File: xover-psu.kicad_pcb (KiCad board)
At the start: 2 copper layers, 100 x 100 mm, 91 parts, among them J1 Screw_Terminal_01x02, J2 Screw_Terminal_01x02, J3 Screw_Terminal_01x02, J4 Screw_Terminal_01x02, J5 Screw_Terminal_01x03, J6 Screw_Terminal_01x02, J7 Screw_Terminal_01x02, J8 Screw_Terminal_01x03, K2 T9GS1L14-12, Q1 AO3400, Q2 2N7002, Q3 AO3400, U1 817C, U2 TL431DBZ, U4 LM317_3PinPackage, U5 LM337_TO220, U6 TL431DBZ, U8 817C

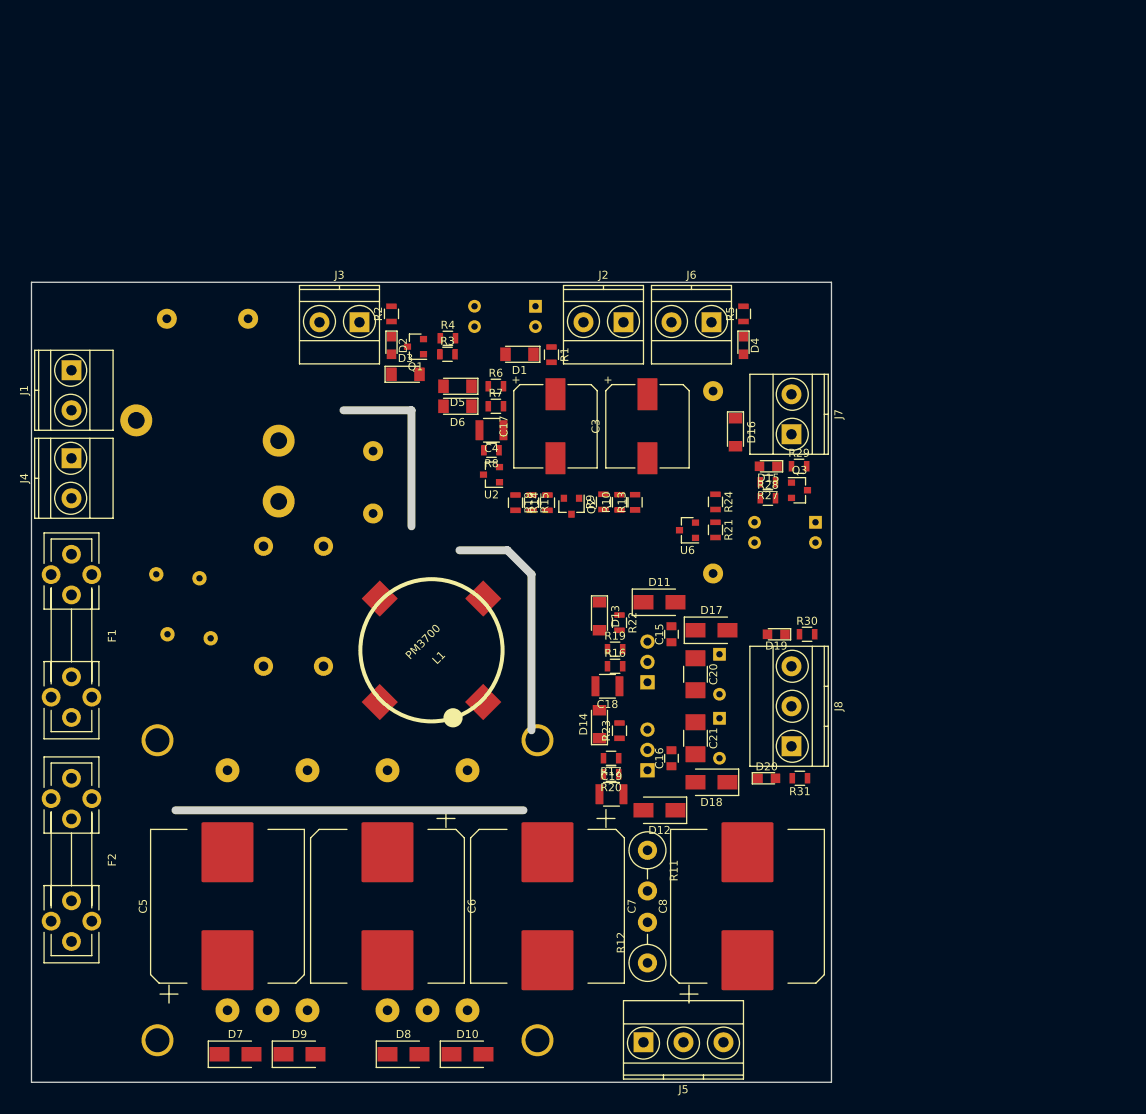
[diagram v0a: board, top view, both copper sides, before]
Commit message: First pass routing completed for all but the UNMUTE timer/logic
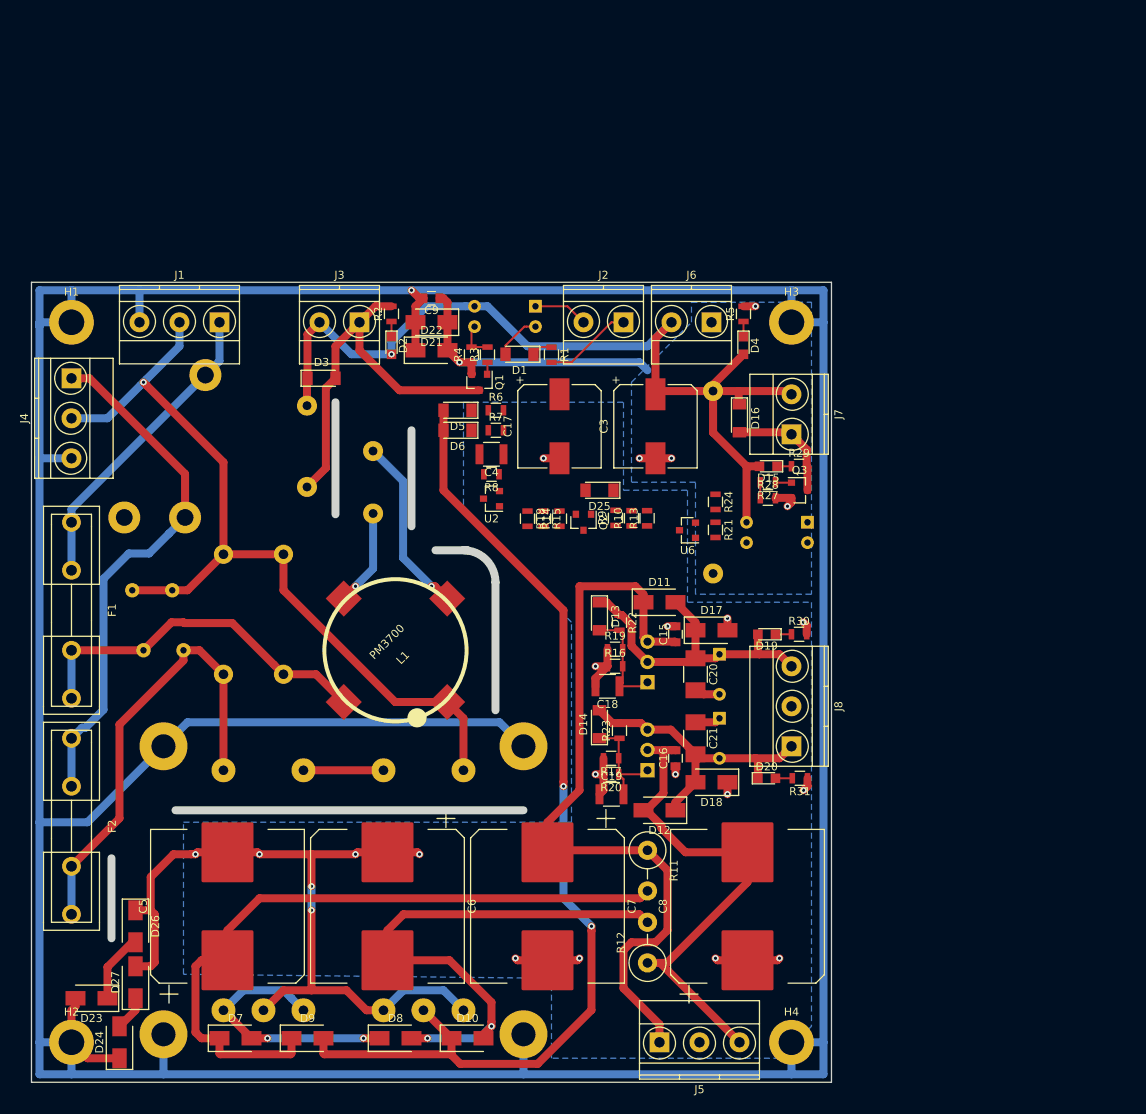
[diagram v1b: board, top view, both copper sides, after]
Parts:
- added C9: 100n, Capacitors_SMD:C_0805, F.Cu at (75.0, 27.0)
- added D21: M7, Diodes_SMD:D_SMA, F.Cu at (75.0, 30.0)
- added D22: M7, Diodes_SMD:D_SMA, F.Cu at (75.0, 33.5)
- added D23: M7, Diodes_SMD:D_SMA, F.Cu at (32.5, 114.5)
- added D24: M7, Diodes_SMD:D_SMA, F.Cu at (36.0, 120.0)
- added D25: LL4148, Diodes_SMD:D_MiniMELF, F.Cu at (96.0, 51.0)
- added D26: M7, Diodes_SMD:D_SMA, F.Cu at (38.0, 105.5)
- added D27: M7, Diodes_SMD:D_SMA, F.Cu at (38.0, 112.5)
- added H1: MountingHole_Pad, Mounting_Holes:MountingHole_3.2mm_M3_DIN965_Pad, F.Cu at (30.0, 30.0)
- added H2: MountingHole_Pad, Mounting_Holes:MountingHole_3.2mm_M3_DIN965_Pad, F.Cu at (30.0, 120.0)
- added H3: MountingHole_Pad, Mounting_Holes:MountingHole_3.2mm_M3_DIN965_Pad, F.Cu at (120.0, 30.0)
- added H4: MountingHole_Pad, Mounting_Holes:MountingHole_3.2mm_M3_DIN965_Pad, F.Cu at (120.0, 120.0)
- F1, F2: footprint Fuse_Holders_and_Fuses:Fuseholder5x20_horiz_open_universal_Type-III -> power:Fuseholder5x20_6mm
- J1, J4: value Screw_Terminal_01x02 -> Screw_Terminal_01x03; footprint Terminals_Phoenix:TerminalBlock_Phoenix_MKDS1.5-2pol -> Terminals_Phoenix:TerminalBlock_Phoenix_MKDS1.5-3pol
- TR1: value TRANSF6 -> TRANSF6_E; footprint pcb:Trafo_CHK-EI54-12VA_Combo -> power:Trafo_CHK-EI54-12VA_Combo_Vigor
- moved J1 19.4 mm to (48.5, 30.0), turned to 180 degrees
- moved D3 10.5 mm to (61.2, 37.0)
- moved J4 10.0 mm to (30.0, 37.0)
- moved RV2 9.22 mm to (44.0, 71.0), turned to 90 degrees
- moved Q1 9.15 mm to (81.0, 37.5), turned to 270 degrees
- moved K2 5.85 mm to (49.0, 45.5), turned to 270 degrees
- moved C1 5.10 mm to (56.5, 74.0)
- moved C2 5.10 mm to (49.0, 74.0)
- moved R3 5.00 mm to (82.0, 34.0), turned to 90 degrees
- moved L1 4.50 mm to (70.5, 71.0)
- moved F2 4.00 mm to (30.0, 83.0)
- moved RV1 3.61 mm to (39.0, 71.0)
- moved R4 3.59 mm to (80.0, 34.0), turned to 90 degrees
- moved C4 3.00 mm to (82.5, 46.5)
- moved D5 3.00 mm to (78.2, 41.0)
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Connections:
- net /12V renamed /VDD
- net Net-(C1-Pad2) renamed /NEUTRAL
- net Net-(C2-Pad1) renamed /PRI
- net Net-(F1-Pad1) renamed /ACTIVE
- net Net-(F2-Pad1) renamed /SWAC
- C15 pad 1: Net-(C15-Pad1) -> /RECT1B
- C16 pad 2: Net-(C16-Pad2) -> /RECT2B
- C7 pad 1: Net-(C15-Pad1) -> /RECT1B
- C8 pad 2: Net-(C16-Pad2) -> /RECT2B
- D11 pad 1: Net-(C15-Pad1) -> /RECT1B
- D12 pad 2: Net-(C16-Pad2) -> /RECT2B
- J5 pad 1: /AC1 -> /RECT1B
- J5 pad 3: /AC2 -> /RECT2B
- R11 pad 1: Net-(C15-Pad1) -> /RECT1B
- R12 pad 1: Net-(C16-Pad2) -> /RECT2B
- R24 pad 1: /RECT2 -> /RECT1B
- R9 pad 2: /RECT2 -> /RECT1B
- U4 pad 3: Net-(C15-Pad1) -> /RECT1B
- U5 pad 2: Net-(C16-Pad2) -> /RECT2B
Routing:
- net /EARTH: track 0.00 -> 532.0 mm, vias 0 -> 1
- net /AGND: track 0.00 -> 142.4 mm, vias 0 -> 19
- net /AC2: track 0.00 -> 129.4 mm, vias 0 -> 2
- net /VDD: track 0.00 -> 118.2 mm, vias 0 -> 1
- net /NEUTRAL: track 0.00 -> 106.8 mm, vias 0 -> 1
- net /RECT1B: track 0.00 -> 96.5 mm
- net /RECT1: track 0.00 -> 87.0 mm
- net /RECT2: track 0.00 -> 68.2 mm, vias 0 -> 2
- net /SWAC: track 0.00 -> 65.8 mm
- net /RECT2B: track 0.00 -> 63.1 mm
- net /PRI: track 0.00 -> 57.0 mm
- net Net-(D3-Pad2): track 0.00 -> 48.7 mm
- net Net-(C1-Pad1): track 0.00 -> 45.6 mm
- net /DGND: track 0.00 -> 45.0 mm, vias 0 -> 5
- net /VCC: track 0.00 -> 40.3 mm
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- added copper zone on B.Cu, net /AGND
- added copper zone on B.Cu, net /DGND
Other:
- outline, holes or cut-outs redrawn
- net class AC added: clearance 2, trace_width 1, via_dia 0.8, via_drill 0.4
- net class DC added: clearance 0.2, trace_width 1, via_dia 0.8, via_drill 0.4
- net class ERF added: clearance 0.2, trace_width 1, via_dia 0.8, via_drill 0.4

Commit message: Fixed transformer phase, made some mains tracks fatter
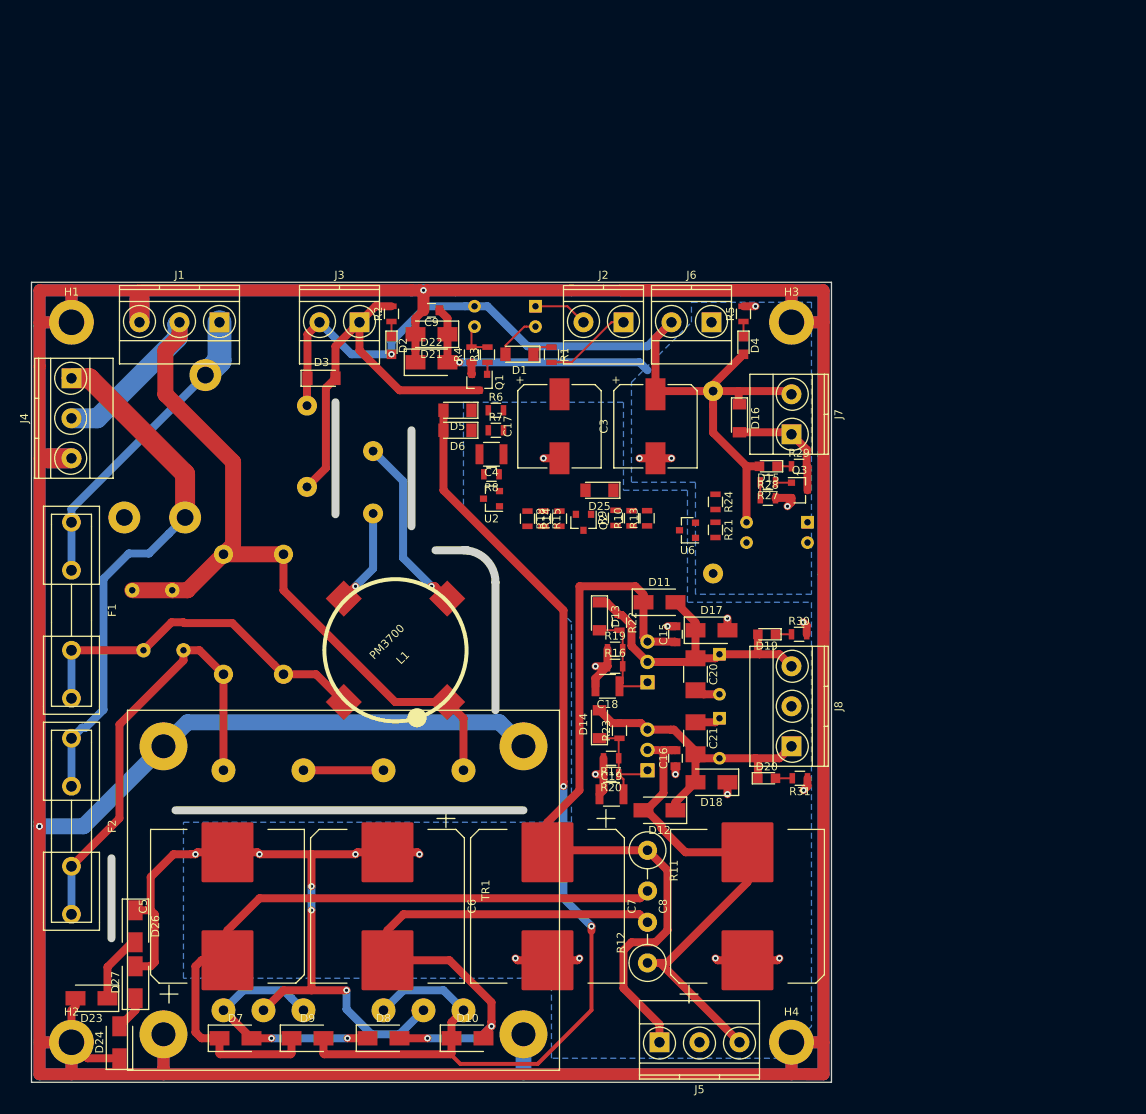
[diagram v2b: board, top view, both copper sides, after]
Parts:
- TR1: moved to F.Cu
- moved C9 1.50 mm to (75.0, 28.5)
- moved D21 1.50 mm to (75.0, 31.5)
- moved D22 1.50 mm to (75.0, 35.0)
- moved D8 1.50 mm to (69.0, 119.5)
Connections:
- TR1 pad 1: /NEUTRAL -> /PRI
- TR1 pad 4: /PRI -> /NEUTRAL
- TR1 pad 5: /AC1 -> /AC2
- TR1 pad 8: /AC2 -> /AC1
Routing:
- net /EARTH: track 532.0 -> 1026.7 mm, vias 1 -> 3
- net /AC2: track 129.4 -> 139.6 mm
- net /NEUTRAL: track 106.8 -> 114.1 mm, vias 1 -> 0
- net /DGND: track 45.0 -> 42.6 mm
- net /AGND: track 142.4 -> 140.2 mm, vias 19 -> 20
- net /RECT2: track 68.2 -> 69.7 mm
- net /AC1: track 33.0 -> 31.5 mm
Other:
- net class ERF: trace_width 1 -> 1.5

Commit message: prettified everything - round corners, readable silkscreens, etc.
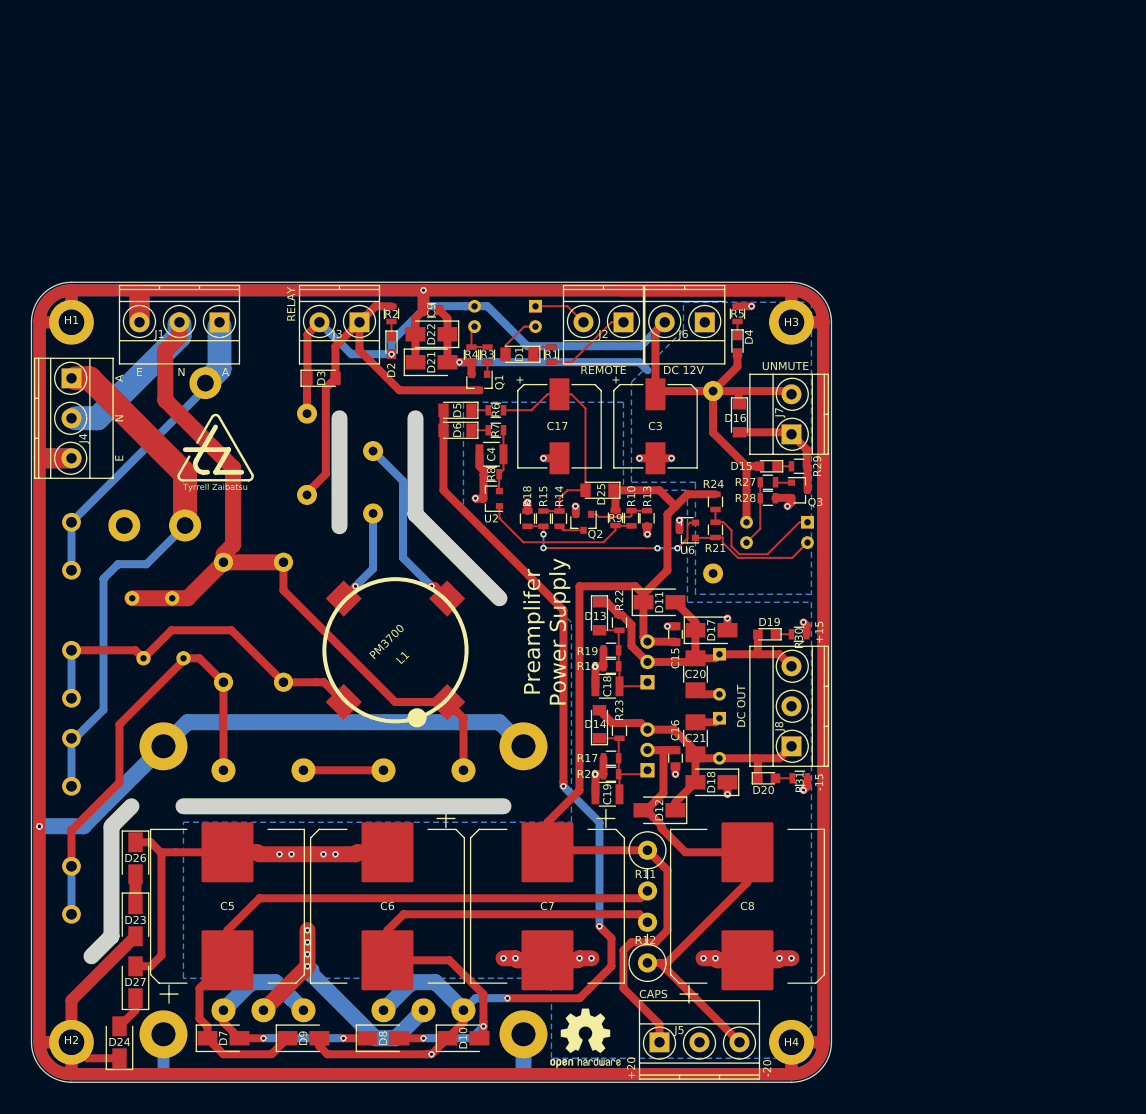
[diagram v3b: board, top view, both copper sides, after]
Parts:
- added REF**: Tyrrell Zaibatsu, tz:Tyrrell-Zaibatsu-20-Back, F.Cu at (114.0, 100.5)
- added REF**: Tyrrell Zaibatsu, tz:Tyrrell-Zaibatsu-10, F.Cu at (48.0, 46.5)
- added REF***: OSHW-Symbol_6.7x6mm_SilkScreen, pcb:OSHW-Symbol_6.7x6mm_BackSilkScreen, F.Cu at (96.0, 118.5)
- added REF***: OSHW-Logo2_9.8x8mm_SilkScreen, Symbols:OSHW-Logo2_9.8x8mm_SilkScreen, F.Cu at (94.2, 119.5)
- F1, F2, TR1: moved to B.Cu
- moved D23 11.2 mm to (38.0, 104.8), turned to 270 degrees
- moved D26 8.50 mm to (38.0, 97.0)
- moved D7 1.50 mm to (49.0, 119.5)
- moved C1 1.00 mm to (56.5, 75.0)
- moved C2 1.00 mm to (49.0, 75.0)
- moved K2 1.00 mm to (49.0, 46.5)
- moved RV1 1.00 mm to (39.0, 72.0)
- moved RV2 1.00 mm to (44.0, 72.0)
- moved J6 0.84 mm to (109.2, 30.0)
- moved D4 0.76 mm to (113.2, 32.8)
- moved R5 0.75 mm to (113.2, 28.9)
- moved R19 0.52 mm to (97.5, 71.0)
- moved C19 0.50 mm to (97.0, 89.0)
- moved D10 0.50 mm to (79.0, 119.5)
- moved D9 0.50 mm to (59.0, 119.5)
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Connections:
- TR1 pad 1: /PRI -> /NEUTRAL
- TR1 pad 4: /NEUTRAL -> /PRI
- TR1 pad 5: /AC2 -> /AC1
- TR1 pad 8: /AC1 -> /AC2
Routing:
- net /EARTH: track 1026.7 -> 928.8 mm
- net /RECT1B: track 96.5 -> 126.0 mm
- net Net-(C17-Pad1): track 0.00 -> 29.3 mm
- net Net-(R15-Pad2): track 0.00 -> 26.0 mm, vias 0 -> 4
- net Net-(R10-Pad1): track 0.00 -> 20.5 mm
- net Net-(R21-Pad1): track 0.00 -> 17.6 mm
- net Net-(R21-Pad2): track 0.00 -> 16.2 mm
- net Net-(C4-Pad1): track 0.00 -> 7.85 mm
- net Net-(Q2-Pad1): track 0.00 -> 7.81 mm
- net Net-(R27-Pad2): track 2.00 -> 8.25 mm
- net /RECT1: track 87.0 -> 81.6 mm
- net Net-(D23-Pad1): track 8.69 -> 3.75 mm
- net /AC2: track 139.6 -> 135.2 mm, vias 2 -> 4
- net Net-(Q2-Pad3): track 0.00 -> 3.21 mm
- net /AGND: track 140.2 -> 143.1 mm, vias 20 -> 30
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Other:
- outline, holes or cut-outs redrawn
- net class ERF: trace_width 1.5 -> 1
- board text added: "+15"
- board text added: "+20"
- board text added: "-15"
- board text added: "-20"
- board text added: "500mA"
- board text added: "817C"
- board text added: "A"
- board text added: "AC LINE"
- board text added: "ACTIVE"
- board text added: "AGND"
- board text added: "CAPS"
- board text added: "DC 12V"
- board text added: "DC IN / CAPS"
- board text added: "DC OUT"
- board text added: "DC12"
- board text added: "DGND"
- board text added: "E"
- board text added: "EARTH"
- board text added: "LM317"
- board text added: "LM337"
- board text added: "N"
- board text added: "NEG"
- board text added: "NEUT"
- board text added: "OD"
- board text added: "POS"
- board text added: "Preamplifer Power Supply"
- board text added: "Preamplifier Power Supply Rev.A 202110 github.com/phenidone"
- board text added: "RELAY"
- board text added: "REMOTE"
- board text added: "SWITCHED AC"
- board text added: "UNMUTE"
- board text added: "VCC"
- board text added: "VDD"
- board text added: "VEE"
